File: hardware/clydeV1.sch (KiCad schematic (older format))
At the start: 4 parts

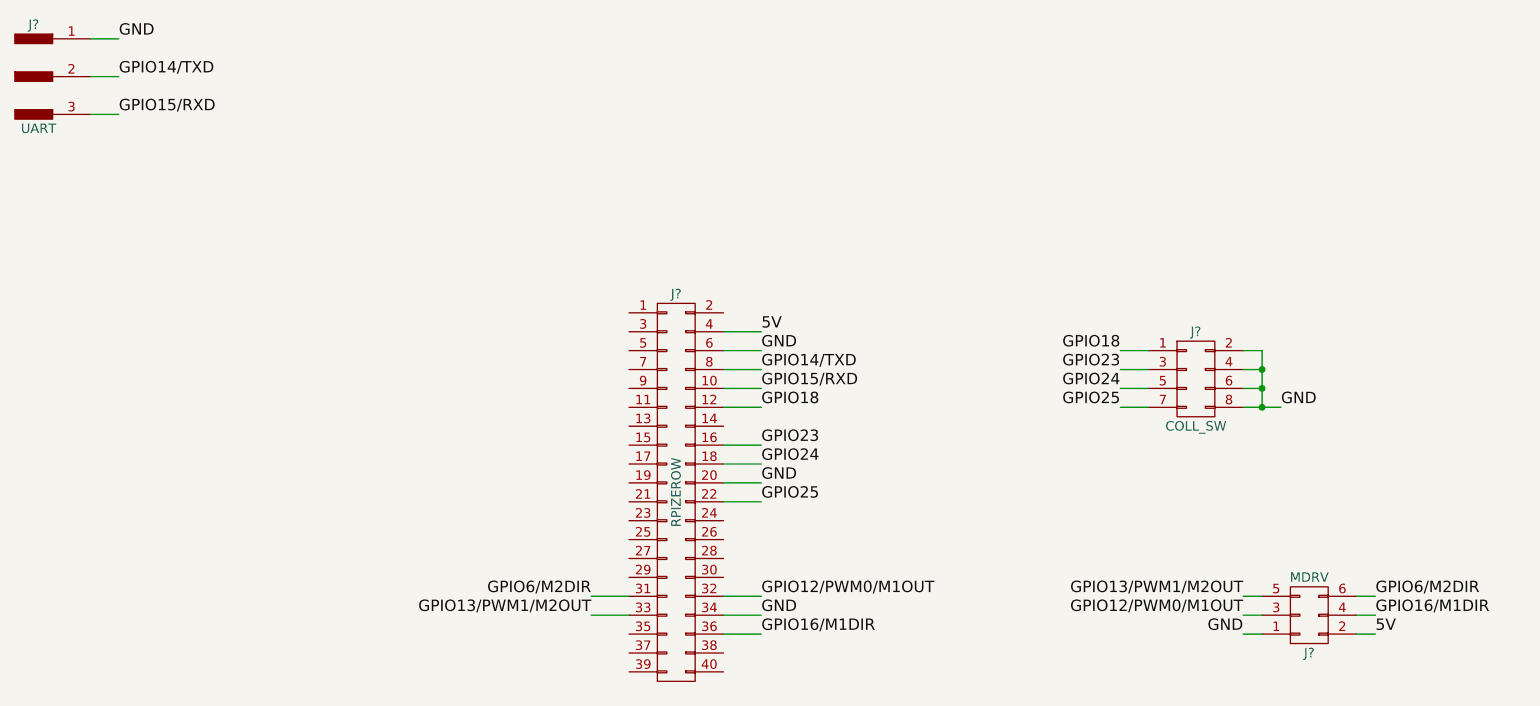
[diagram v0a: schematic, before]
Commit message: HARDWARE: add pcb layout
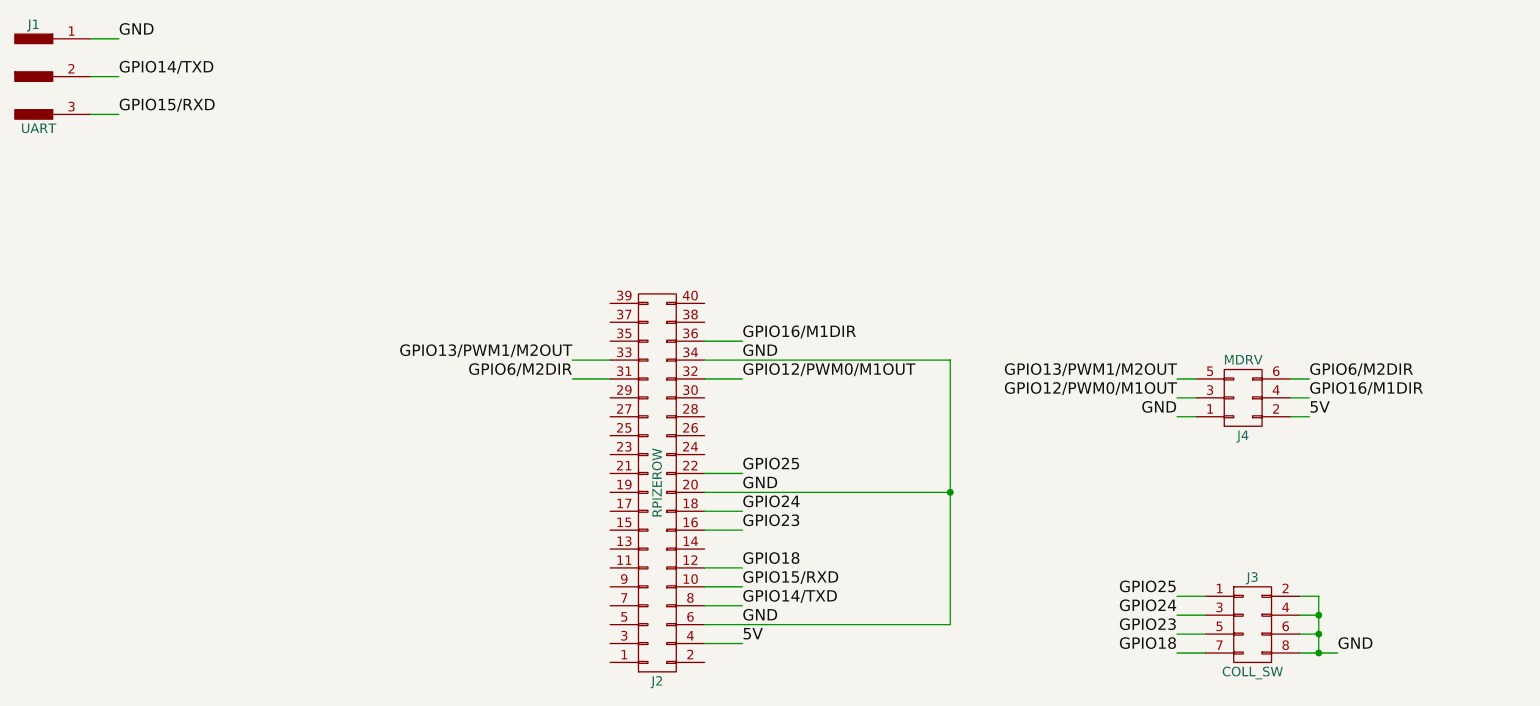
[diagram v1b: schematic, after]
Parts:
- J1: renamed from J?; footprint (none) -> Pin_Headers:Pin_Header_Angled_1x03_Pitch2.54mm
- J2: renamed from J?; footprint (none) -> Socket_Strips:Socket_Strip_Straight_2x20_Pitch2.54mm
- J3: renamed from J?; footprint (none) -> Pin_Headers:Pin_Header_Angled_2x04_Pitch2.54mm
- J4: renamed from J?; footprint (none) -> Pin_Headers:Pin_Header_Angled_2x03_Pitch2.54mm
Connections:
- net GPIO18: now also J3.7 (P7); no longer J3.1 (P1)
- net GPIO23: now also J3.5 (P5); no longer J3.3 (P3)
- net GPIO24: now also J3.3 (P3); no longer J3.5 (P5)
- net GPIO25: now also J3.1 (P1); no longer J3.7 (P7)
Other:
- moved on the sheet: J2, J3, J4
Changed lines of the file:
@@
 LIBS:contrib
 LIBS:valves
+LIBS:clydeV1-cache
 EELAYER 25 0
 EELAYER END
@@
 $EndDescr
 $Comp
-L CONN_02X20 J?
+L CONN_02X20 J2
 U 1 1 59997E0D
-P 5200 3900
-F 0 "J?" H 5200 4950 50  0000 C CNN
-F 1 "RPIZEROW" V 5200 3900 50  0000 C CNN
-F 2 "" H 5200 2950 50  0001 C CNN
-F 3 "" H 5200 2950 50  0001 C CNN
-	1    5200 3900
-	1    0    0    -1
+P 5100 3850
+F 0 "J2" H 5100 4900 50  0000 C CNN
+F 1 "RPIZEROW" V 5100 3850 50  0000 C CNN
+F 2 "Socket_Strips:Socket_Strip_Straight_2x20_Pitch2.54mm" H 5100 2900 50  0001 C CNN
+F 3 "" H 5100 2900 50  0001 C CNN
+	1    5100 3850
+	1    0    0    1
 $EndComp
 Wire Wire Line
-	5450 3150 5650 3150
-Text Label 5650 3150 0    60   ~ 0
+	6650 4600 5350 4600
+Text Label 5550 4600 0    60   ~ 0
 GND
 Wire Wire Line
-	5450 3250 5650 3250
-Text Label 5650 3250 0    60   ~ 0
+	5350 4500 5550 4500
+Text Label 5550 4500 0    60   ~ 0
 GPIO14/TXD
 Wire Wire Line
-	5450 3350 5650 3350
-Text Label 5650 3350 0    60   ~ 0
+	5350 4400 5550 4400
+Text Label 5550 4400 0    60   ~ 0
 GPIO15/RXD
 $Comp
-L CONN_01X03_MALE J?
+L CONN_01X03_MALE J1
 U 1 1 59997F6D
 P 1800 1700
-F 0 "J?" H 1800 1975 50  0000 C CNN
+F 0 "J1" H 1800 1975 50  0000 C CNN
 F 1 "UART" H 1825 1425 50  0000 C CNN
-F 2 "" H 1800 1900 50  0001 C CNN
+F 2 "Pin_Headers:Pin_Header_Angled_1x03_Pitch2.54mm" H 1800 1900 50  0001 C CNN
 F 3 "" H 1800 1900 50  0001 C CNN
 	1    1800 1700
@@
 GPIO15/RXD
 $Comp
-L CONN_02X03 J?
+L CONN_02X03 J4
 U 1 1 599980F6
-P 8550 4550
-F 0 "J?" H 8550 4750 50  0000 C CNN
-F 1 "MDRV" H 8550 4350 50  0000 C CNN
-F 2 "" H 8550 3350 50  0001 C CNN
-F 3 "" H 8550 3350 50  0001 C CNN
-	1    8550 4550
+P 8200 3400
+F 0 "J4" H 8200 3600 50  0000 C CNN
+F 1 "MDRV" H 8200 3200 50  0000 C CNN
+F 2 "Pin_Headers:Pin_Header_Angled_2x03_Pitch2.54mm" H 8200 2200 50  0001 C CNN
+F 3 "" H 8200 2200 50  0001 C CNN
+	1    8200 3400
 	1    0    0    1
 $EndComp
 $Comp
-L CONN_02X04 J?
+L CONN_02X04 J3
 U 1 1 5999816B
-P 7950 3300
-F 0 "J?" H 7950 3550 50  0000 C CNN
-F 1 "COLL_SW" H 7950 3050 50  0000 C CNN
-F 2 "" H 7950 2100 50  0001 C CNN
-F 3 "" H 7950 2100 50  0001 C CNN
-	1    7950 3300
+P 8250 4600
+F 0 "J3" H 8250 4850 50  0000 C CNN
+F 1 "COLL_SW" H 8250 4350 50  0000 C CNN
+F 2 "Pin_Headers:Pin_Header_Angled_2x04_Pitch2.54mm" H 8250 3400 50  0001 C CNN
+F 3 "" H 8250 3400 50  0001 C CNN
+	1    8250 4600
 	1    0    0    -1
 $EndComp
 Wire Wire Line
-	5450 3450 5650 3450
+	5350 4300 5550 4300
 Wire Wire Line
-	5450 3650 5650 3650
+	5350 4100 5550 4100
 Wire Wire Line
-	5450 3750 5650 3750
+	5350 4000 5550 4000
 Wire Wire Line
-	5450 3950 5650 3950
-Text Label 5650 3450 0    60   ~ 0
+	5350 3800 5550 3800
+Text Label 5550 4300 0    60   ~ 0
 GPIO18
-Text Label 5650 3650 0    60   ~ 0
+Text Label 5550 4100 0    60   ~ 0
 GPIO23
-Text Label 5650 3750 0    60   ~ 0
+Text Label 5550 4000 0    60   ~ 0
 GPIO24
-Text Label 5650 3950 0    60   ~ 0
+Text Label 5550 3800 0    60   ~ 0
 GPIO25
 Wire Wire Line
-	5450 3850 5650 3850
-Text Label 5650 3850 0    60   ~ 0
+	5350 3900 6650 3900
+Text Label 5550 3900 0    60   ~ 0
 GND
 Wire Wire Line
-	7700 3150 7550 3150
+	8000 4750 7850 4750
 Wire Wire Line
-	7700 3250 7550 3250
+	8000 4650 7850 4650
 Wire Wire Line
-	7700 3350 7550 3350
+	8000 4550 7850 4550
 Wire Wire Line
-	7700 3450 7550 3450
-Text Label 7550 3150 2    60   ~ 0
+	8000 4450 7850 4450
+Text Label 7850 4750 2    60   ~ 0
 GPIO18
-Text Label 7550 3250 2    60   ~ 0
+Text Label 7850 4650 2    60   ~ 0
 GPIO23
-Text Label 7550 3350 2    60   ~ 0
+Text Label 7850 4550 2    60   ~ 0
 GPIO24
-Text Label 7550 3450 2    60   ~ 0
+Text Label 7850 4450 2    60   ~ 0
 GPIO25
 Wire Wire Line
-	8200 3150 8300 3150
+	8500 4450 8600 4450
 Wire Wire Line
-	8200 3250 8300 3250
+	8500 4550 8600 4550
 Wire Wire Line
-	8300 3350 8200 3350
+	8600 4650 8500 4650
 Wire Wire Line
-	8200 3450 8400 3450
+	8500 4750 8700 4750
 Wire Wire Line
-	8300 3150 8300 3450
-Connection ~ 8300 3250
-Connection ~ 8300 3450
-Connection ~ 8300 3350
-Text Label 8400 3450 0    60   ~ 0
+	8600 4450 8600 4750
+Connection ~ 8600 4550
+Connection ~ 8600 4750
+Connection ~ 8600 4650
+Text Label 8700 4750 0    60   ~ 0
 GND
 Wire Wire Line
-	4950 4450 4750 4450
+	4850 3300 4650 3300
 Wire Wire Line
-	4950 4550 4750 4550
+	4850 3200 4650 3200
 Wire Wire Line
-	5450 4450 5650 4450
+	5350 3300 5550 3300
 Wire Wire Line
-	5450 4550 5650 4550
+	5350 3200 6650 3200
 Wire Wire Line
-	5450 4650 5650 4650
-Text Label 5650 4550 0    60   ~ 0
+	5350 3100 5550 3100
+Text Label 5550 3200 0    60   ~ 0
 GND
-Text Label 5650 4450 0    60   ~ 0
+Text Label 5550 3300 0    60   ~ 0
 GPIO12/PWM0/M1OUT
-Text Label 4750 4550 2    60   ~ 0
+Text Label 4650 3200 2    60   ~ 0
 GPIO13/PWM1/M2OUT
-Text Label 4750 4450 2    60   ~ 0
+Text Label 4650 3300 2    60   ~ 0
 GPIO6/M2DIR
-Text Label 5650 4650 0    60   ~ 0
+Text Label 5550 3100 0    60   ~ 0
 GPIO16/M1DIR
 Wire Wire Line
-	8300 4450 8200 4450
+	7950 3300 7850 3300
 Wire Wire Line
-	8300 4550 8200 4550
+	7950 3400 7850 3400
 Wire Wire Line
-	8300 4650 8200 4650
+	7950 3500 7850 3500
 Wire Wire Line
-	8800 4450 8900 4450
+	8450 3300 8550 3300
 Wire Wire Line
-	8800 4550 8900 4550
+	8450 3400 8550 3400
 Wire Wire Line
-	8800 4650 8900 4650
-Text Label 8200 4650 2    60   ~ 0
+	8450 3500 8550 3500
+Text Label 7850 3500 2    60   ~ 0
 GND
-Text Label 8200 4550 2    60   ~ 0
+Text Label 7850 3400 2    60   ~ 0
 GPIO12/PWM0/M1OUT
-Text Label 8200 4450 2    60   ~ 0
+Text Label 7850 3300 2    60   ~ 0
 GPIO13/PWM1/M2OUT
-Text Label 8900 4450 0    60   ~ 0
+Text Label 8550 3300 0    60   ~ 0
 GPIO6/M2DIR
-Text Label 8900 4550 0    60   ~ 0
+Text Label 8550 3400 0    60   ~ 0
 GPIO16/M1DIR
-Text Label 8900 4650 0    60   ~ 0
+Text Label 8550 3500 0    60   ~ 0
 5V
 Wire Wire Line
-	5450 3050 5650 3050
-Text Label 5650 3050 0    60   ~ 0
+	5350 4700 5550 4700
+Text Label 5550 4700 0    60   ~ 0
 5V
+Wire Wire Line
+	6650 3200 6650 4600
+Connection ~ 6650 3900
 $EndSCHEMATC

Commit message: HARDWARE: update circuit diagram
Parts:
- added C1, C2: C, symbol C
- added D1, D2: LED, symbol LED
- added J5: USB_OTG, symbol USB_OTG
- added LS1: Speaker, symbol Speaker
- added M1, M2: Motor_DC, symbol Motor_DC
- added R1, R10, R11, R12, R13, R14, R2, R3, R4, R5, R6, R7, R8, R9: R, symbol R
- added SW1, SW2: SW_DPDT_x2, symbol SW_DPDT_x2
- added U1, U2: TIL111, Housings_DIP:DIP-6_W7.62mm, symbol TIL111
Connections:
- net labels added: 3V3, ENC_1, ENC_2, GPIO17/LED1, GPIO26/ENC_1, GPIO27/LED2, GPIO4/SPK, GPIO5/ENC_2, LED1, LED2, M1DIR, M1OUT, M1_A, M1_B, M2DIR, M2OUT, M2_A, M2_B, N.C., SPK, SW_1, SW_2, SW_3, SW_4
- wire segments 33 -> 152
- no-connect marks 0 -> 4
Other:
- note added: "Clyde: A Room Mapping Robot"
- note added: "Inputs"
- note added: "Motor Driver 1"
- note added: "Motor Driver 2"
- note added: "Outputs"
- note added: "Powerbank"
- note added: "Raspberry Pi"
- moved on the sheet: J1, J3, J4
